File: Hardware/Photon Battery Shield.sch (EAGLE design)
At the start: 22 parts, among them J1 POWER_JACKSMD, U1 MCP73831, U2 MAX1704X

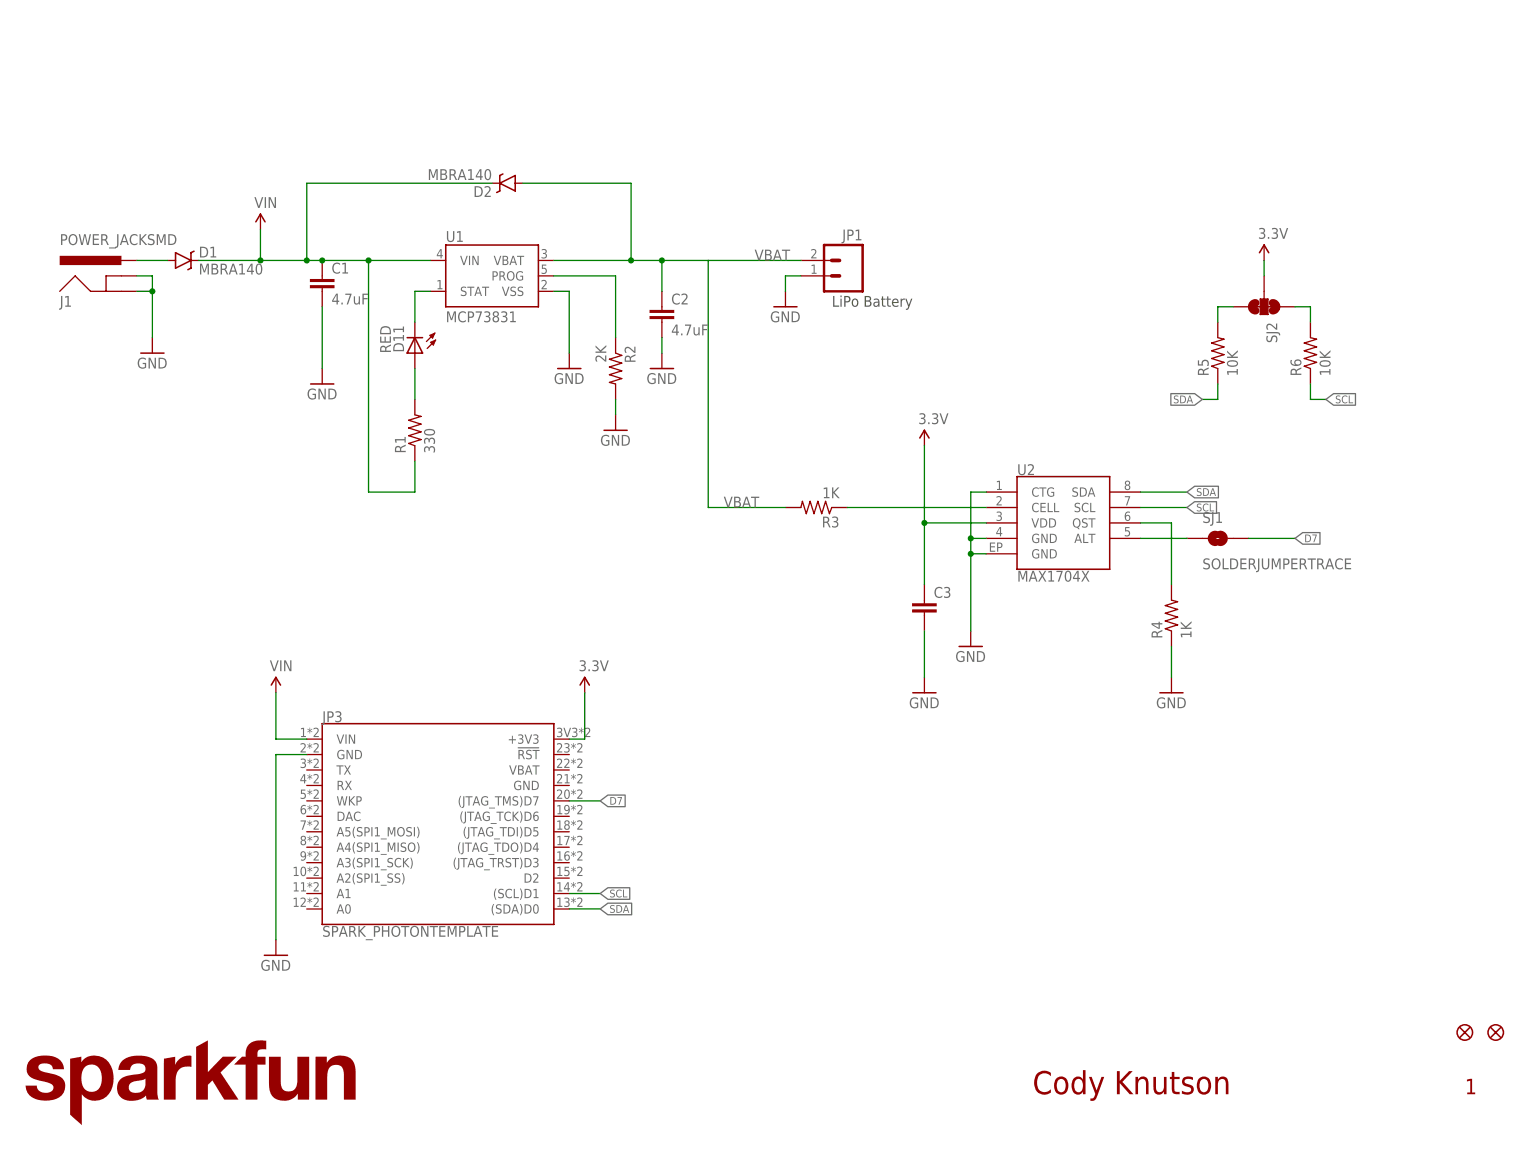
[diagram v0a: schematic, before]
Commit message: Adjusting VIN route, GND vias. Checklist stuff.
- Adding measures
- Adding PROD_ID to some parts
- Re-routed ALERT pin to D6
- Added MAx17043 i2c address to schematic
- Labeled jumpers ("Pullups" and "Alert")
- Routed traces from fuel gauge directly out of pads. (Added tRestrict to
  make sure GND traces didn't come out sides.)
- Labeled LED "CHG"
- Re-sized "5V" silk
- Changed version number to "v01", added to b copper
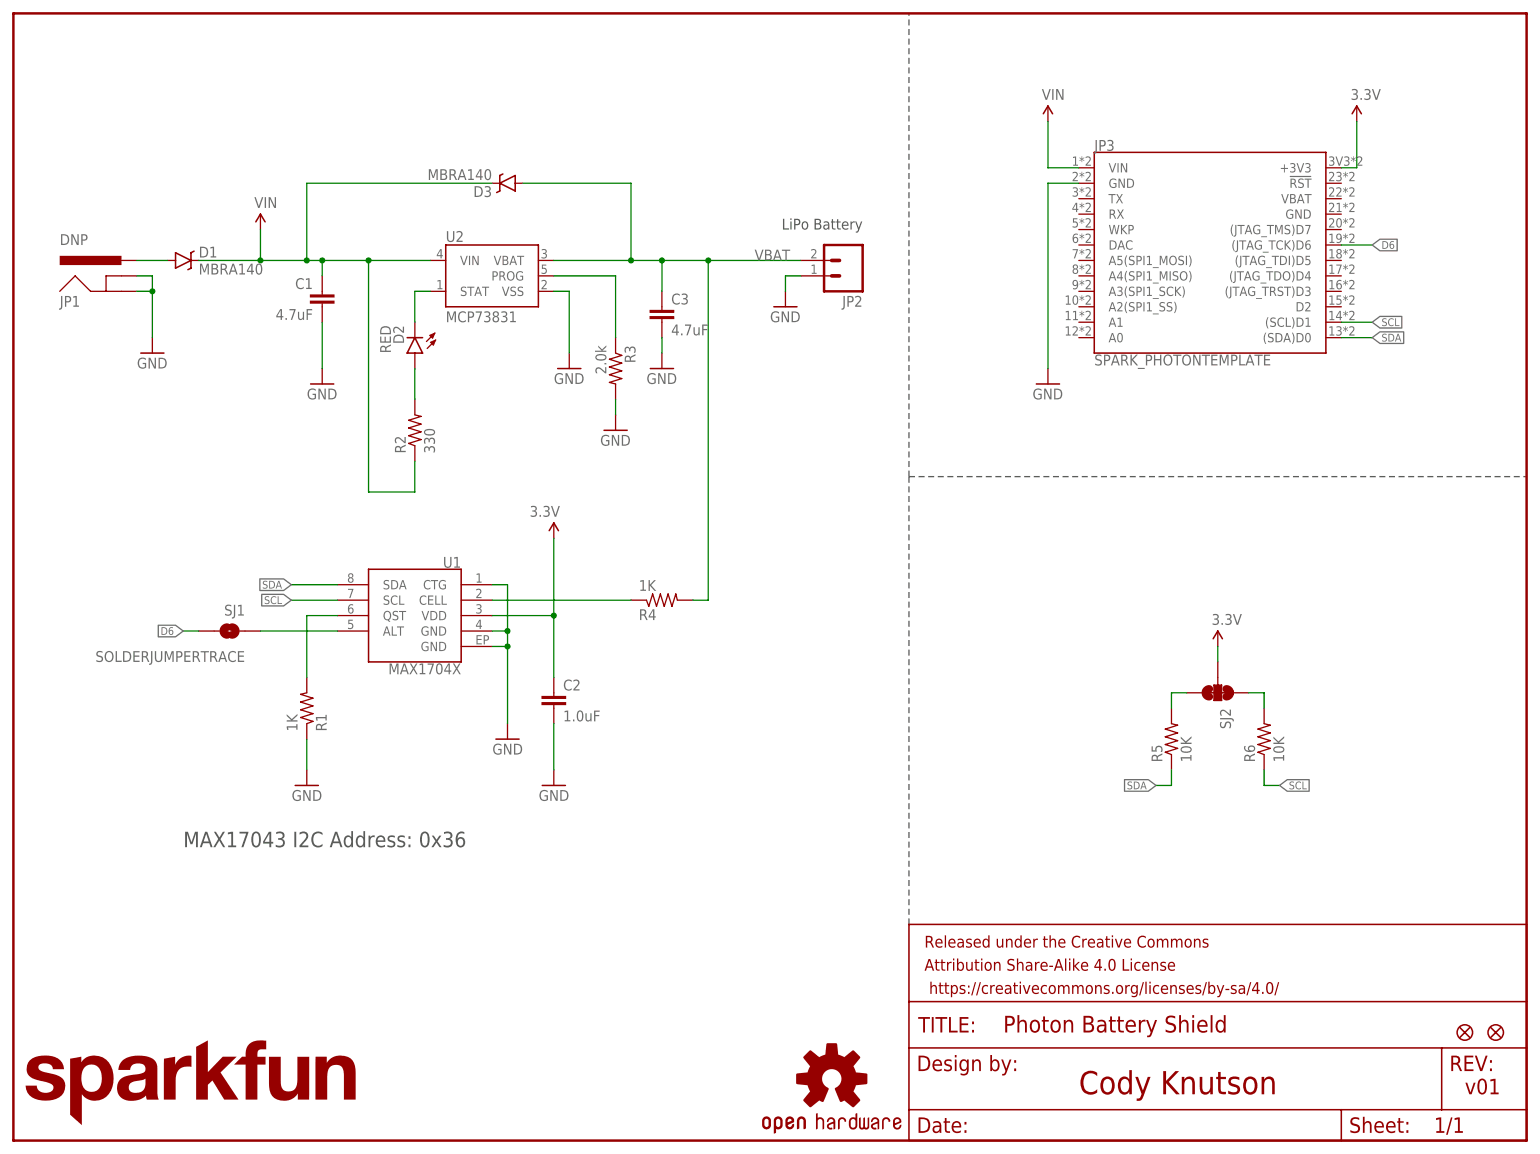
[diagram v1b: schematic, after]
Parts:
- removed D11: RED, SparkFun-LED:LED0603
- removed J1: POWER_JACKSMD, SparkFun-Connectors:POWER_JACKSMD
- added D3: MBRA140, SparkFun-DiscreteSemi:DIODE-SCHOTTKY-MBRA140
- added FRAME1: (no value), SparkFun-Aesthetics:FRAME-LETTER
- added JP2: (no value), SparkFun-Connectors:M02-JST-2MM-SMT
- added LOGO2: OSHW-LOGOS, SparkFun-Aesthetics:OSHW-LOGOS
- C1: device SparkFun-Passives:CAP0603-CAP -> SparkFun-Capacitors:4.7UF-6.3V-10%(0603)0603
- C2: value 4.7uF -> 1.0uF; device SparkFun-Passives:CAP0603-CAP -> SparkFun-Capacitors:1.0UF-16V-10%(0603)
- C3: value (none) -> 4.7uF; device SparkFun-Passives:CAP0603-CAP -> SparkFun-Capacitors:4.7UF-6.3V-10%(0603)0603
- D2: value MBRA140 -> RED; device SparkFun-DiscreteSemi:DIODE-SCHOTTKY-MBRA140 -> SparkFun-LED:LED-RED0603
- JP1: value (none) -> DNP; device SparkFun-Connectors:M02-JST-2MM-SMT -> SparkFun-Connectors:POWER_JACKSMD
- R1: value 330 -> 1K; device SparkFun-Passives:RESISTOR0603-RES -> SparkFun-Resistors:1KOHM-1/10W-1%(0603)
- R2: value 2K -> 330; device SparkFun-Passives:RESISTOR0603-RES -> SparkFun-Resistors:330OHM1/10W1%(0603)
- R3: value 1K -> 2.0k; device SparkFun-Passives:RESISTOR0603-RES -> SparkFun-Resistors:2.0KOHM1/10W5%(0603)
- R4: device SparkFun-Passives:RESISTOR0603-RES -> SparkFun-Resistors:1KOHM-1/10W-1%(0603)
- U1: value MCP73831 -> MAX1704X; device SparkFun-PowerIC:MCP73831 -> SparkFun-PowerIC:MAX1704X
- U2: value MAX1704X -> MCP73831; device SparkFun-PowerIC:MAX1704X -> SparkFun-PowerIC:MCP73831
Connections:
- removed net D7: JP3.(JTAG_TMS)D7, SJ1.2
- new net D6: JP3.(JTAG_TCK)D6, SJ1.2
- net 3.3V: now also C2.1, U1.VDD; no longer C3.1, U2.VDD
- net GND: now also JP1.GND, JP1.GNDBREAK, JP2.2, R1.1, R3.2, U1.CTG, U1.GND@4, U1.GND@EP, U2.VSS; no longer J1.GND, J1.GNDBREAK, JP1.1, R2.2, R4.1, U1.VSS, U2.CTG, U2.GND@4, U2.GND@EP
- net N$1: now also D2.A, R2.2; no longer D11.A, R1.2
- net N$2: now also D2.C, U2.STAT; no longer D11.C, U1.STAT
- net N$3: now also R3.1, U2.PROG; no longer R2.1, U1.PROG
- net N$4: now also U1.ALT; no longer U2.ALT
- net N$5: now also R4.1, U1.CELL; no longer R3.1, U2.CELL
- net N$6: now also R1.2, U1.QST; no longer R4.2, U2.QST
- net N$8: now also JP1.PWR; no longer J1.PWR
- net SCL: now also U1.SCL; no longer U2.SCL
- net SDA: now also U1.SDA; no longer U2.SDA
- net VBAT: now also C3.1, D3.A, JP2.1, R4.2, U2.VBAT; no longer C2.1, D2.A, JP1.2, R3.2, U1.VBAT
- net VIN: now also D3.C, R2.1, U2.VIN; no longer D2.C, R1.1, U1.VIN
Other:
- note added: "MAX17043 I2C Address: 0x36"
- note added: "v01"
- note removed: "1"
- moved on the sheet: C1, C2, C3, JP1, JP3, R1, R2, R3, R4, R5, R6, SJ1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

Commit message: Checklist Fixes
(1) Added input voltage label on SCH

(2) Added description for SJ1 in SCH

(3) Added description for SJ2 in SCH

(4) Fixed traces on R2, D1, and STAT pad on MCP

(5) 3-way pull up now has SDA and SCL BPlace objects added next to the
jumper

(6) Resized Board Name text objects to prevent overlap with VBAT text
object

(7) "CHG" TPlace text, and the "Pull-ups" and "ALERT" BPlace text
objects have been changed to Vector font type.
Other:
- note added: "5v Input"
- note added: "Cut jumper to detach Alert from D6"
- note added: "Pullups for I2C on the MCP73831 (Cut to Disable)"
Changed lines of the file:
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@@
 <?xml version="1.0" encoding="utf-8"?>
 <!DOCTYPE eagle SYSTEM "eagle.dtd">
-<eagle version="7.1.0">
+<eagle version="7.2.0">
 <drawing>
 <settings>
@@
 <wire x1="104.14" y1="93.98" x2="205.74" y2="93.98" width="0.2032" layer="97" style="shortdash"/>
 <text x="-15.24" y="33.02" size="2.54" layer="97">MAX17043 I2C Address: 0x36</text>
+<text x="-12.7" y="142.24" size="1.778" layer="97" rot="MR0">5v Input</text>
+<text x="-35.56" y="60.96" size="1.27" layer="97">Cut jumper to detach Alert from D6</text>
+<text x="139.7" y="35.56" size="1.27" layer="97">Pullups for I2C on the MCP73831
+(Cut to Disable)</text>
 </plain>
 <instances>

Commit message: Connecting GND - Photon pin 21 - to the GND plane.
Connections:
- net GND: now also JP3.GND@21
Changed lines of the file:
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@@
 <?xml version="1.0" encoding="utf-8"?>
 <!DOCTYPE eagle SYSTEM "eagle.dtd">
-<eagle version="7.2.0">
+<eagle version="7.1.0">
 <drawing>
 <settings>
@@
 <part name="FID2" library="SparkFun-Aesthetics" deviceset="FIDUCIAL" device="1X2"/>
 <part name="LOGO2" library="SparkFun-Aesthetics" deviceset="OSHW-LOGO" device="S"/>
+<part name="GND11" library="SparkFun-Aesthetics" deviceset="GND" device=""/>
 </parts>
 <sheets>
@@
 <instance part="FID2" gate="G$1" x="200.66" y="2.54" rot="R90"/>
 <instance part="LOGO2" gate="G$1" x="91.44" y="-5.08"/>
+<instance part="GND11" gate="1" x="177.8" y="109.22"/>
 </instances>
 <busses>
@@
 <junction x="-20.32" y="124.46"/>
 </segment>
+<segment>
+<pinref part="JP3" gate="G$1" pin="GND@21"/>
+<wire x1="175.26" y1="137.16" x2="177.8" y2="137.16" width="0.1524" layer="91"/>
+<wire x1="177.8" y1="137.16" x2="177.8" y2="111.76" width="0.1524" layer="91"/>
+<pinref part="GND11" gate="1" pin="GND"/>
+</segment>
 </net>

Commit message: Updating Photon package to WIDE footprint. Defaulting SJ1 to open.
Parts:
- removed LOGO1: SFE_LOGO_NAME.1_INCH, SparkFun-Aesthetics:SFE_LOGO_NAME.1_INCH
- added LOGO3: SFE_LOGO_NAME_FLAME.1_INCH, SparkFun-Aesthetics:SFE_LOGO_NAME_FLAME.1_INCH
- JP3: value SPARK_PHOTONTEMPLATE -> SPARK_PHOTONTEMPLATE_WIDE; device template_temp:SPARK_PHOTONTEMPLATE -> template_temp:SPARK_PHOTONTEMPLATE_WIDE
- SJ1: value SOLDERJUMPERTRACE -> alert; device SparkFun-Passives:SOLDERJUMPERTRACE -> SparkFun-Passives:JUMPER-PAD-2-NOYES_SILK
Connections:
- net D6: now also SJ1.1; no longer SJ1.2
- net N$4: now also SJ1.2; no longer SJ1.1
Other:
- note added: "Cody Knutson Jim Lindblom"
- note added: "Solder jumper to connect Alert to D6"
- note added: "v10"
- note removed: "Cody Knutson"
- note removed: "Cut jumper to detach Alert from D6"
- note removed: "v01"
